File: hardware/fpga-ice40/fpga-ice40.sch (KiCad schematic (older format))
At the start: 74 parts, among them J1 MicroSD_Molex_1040310811, J2 ProgHeader_iCE40, J3 ProgHeader_Flash_QSPI, U1 iCE40HX4K-TQ144, U2 IS42S16320F-6TL, U3 W25Q32JVZP, U4 W25Q32JVZP

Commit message: Use a combined SOIC-8/16W layout for flash ICs
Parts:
- removed U3, U4: W25Q32JVZP, Package_SON:WSON-8-1EP_6x5mm_P1.27mm_EP3.4x4.3mm, symbol ng_memory:W25Q32JVZP
- added U3, U4: W25Q32JVSS, Package_SO:SOIC-8_5.275x5.275mm_P1.27mm, symbol ng_memory:W25Q32JVSS
- added U5, U6: S25FL256SAGMFI01, Package_SO:SOIC-16W_7.5x10.3mm_P1.27mm, symbol ng_memory:S25FL256SAGMFI01
- gave numbers to parts that had none: 37
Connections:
- wire segments 356 -> 374
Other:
- moved on the sheet: C22, C23, C24, J1, J2, J3, R8, RN1, RN2, RN3

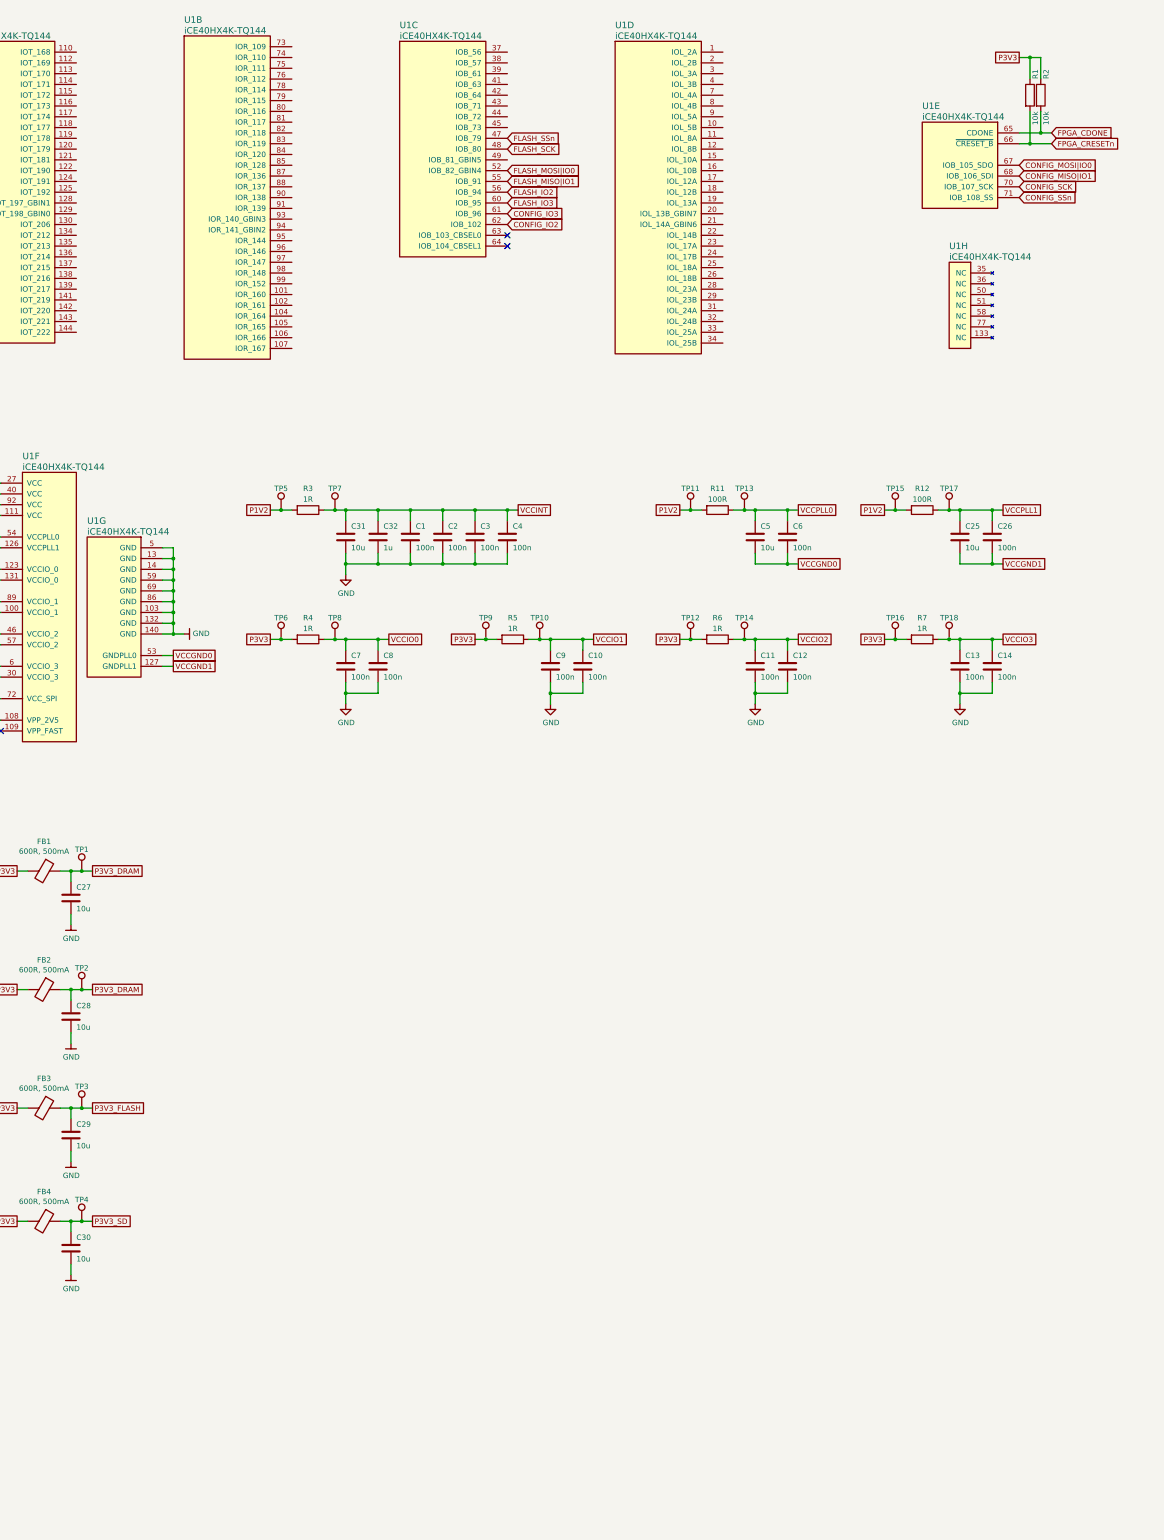
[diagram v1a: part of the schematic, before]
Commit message: Begin pin assignments from FPGA to N64 bus and SDRAM
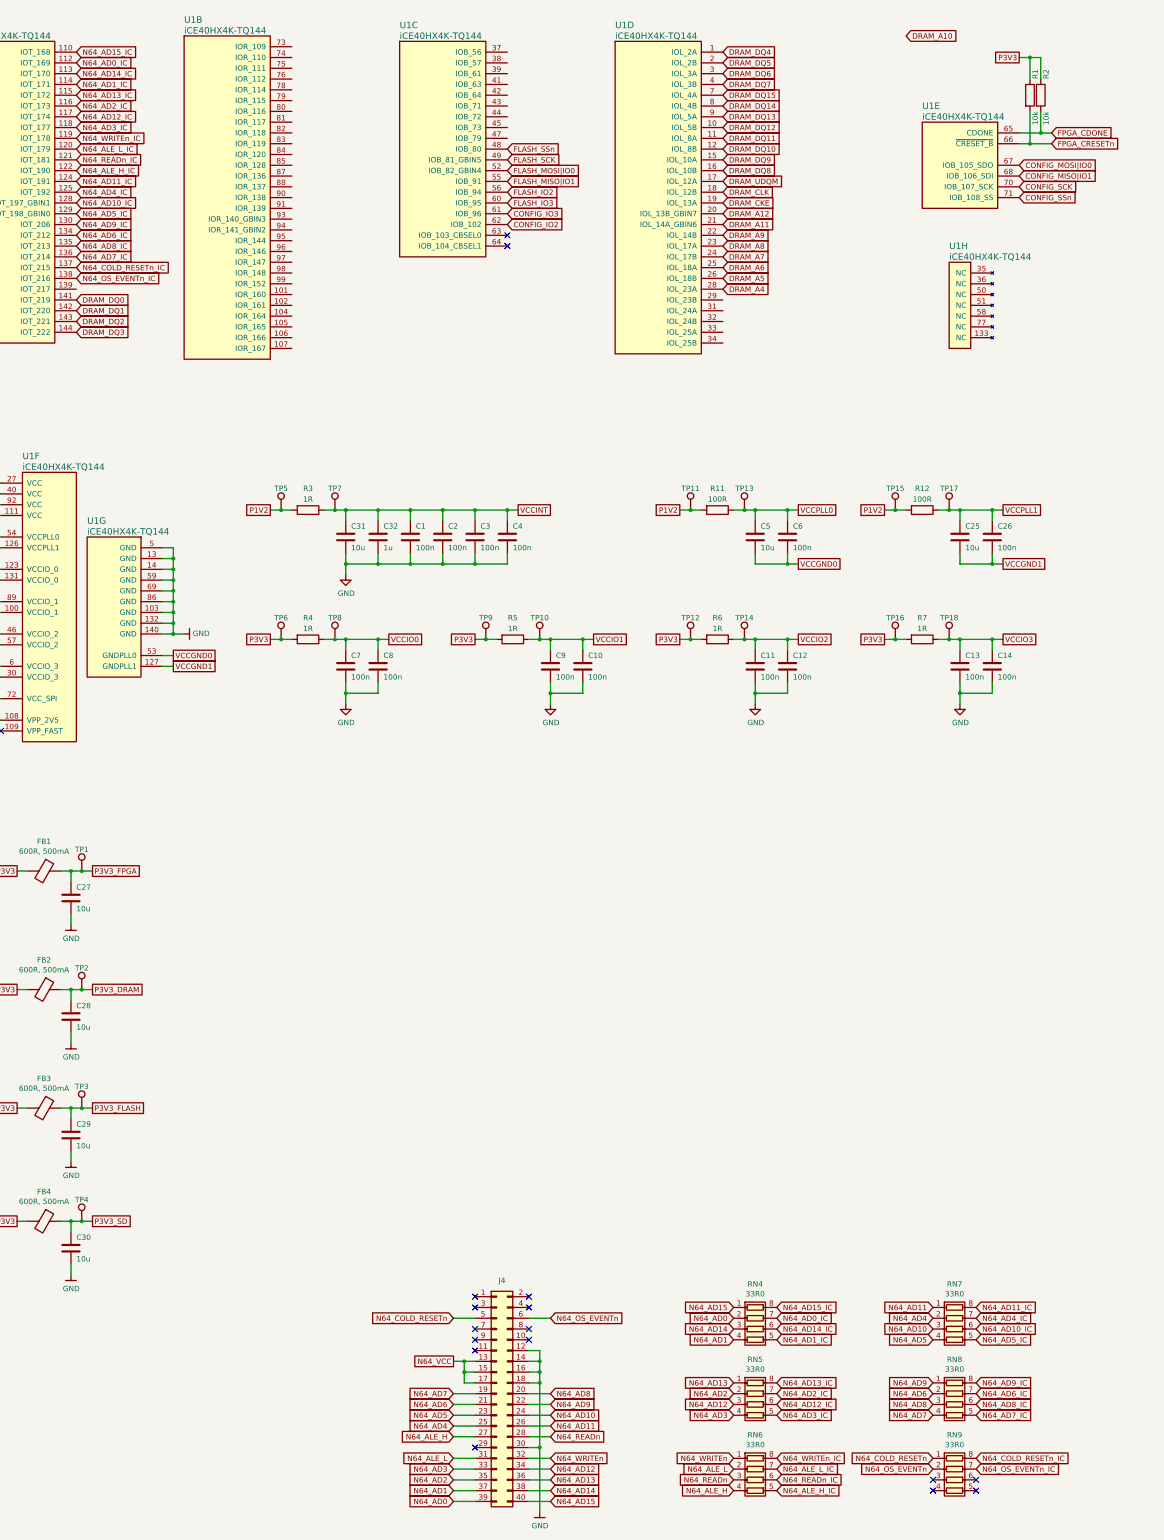
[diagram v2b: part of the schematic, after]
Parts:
- added J4: Conn_02x20_Odd_Even, Connector_PinHeader_2.54mm:PinHeader_2x20_P2.54mm_Horizontal, symbol Connector_Generic:Conn_02x20_Odd_Even
- added RN4, RN5, RN6, RN7, RN8, RN9: 33R0, Resistor_SMD:R_Array_Convex_4x0603, symbol Device:R_Pack04
- RN1, RN2, RN3: footprint (none) -> Resistor_SMD:R_Array_Convex_4x0603
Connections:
- net DRAM_A11: now also U1.21 (IOL_14A_GBIN6)
- net DRAM_A12: now also U1.20 (IOL_13B_GBIN7)
- net DRAM_A4: now also U1.28 (IOL_23A)
- net DRAM_A5: now also U1.26 (IOL_18B)
- net DRAM_A6: now also U1.25 (IOL_18A)
- net DRAM_A7: now also U1.24 (IOL_17B)
- net DRAM_A8: now also U1.23 (IOL_17A)
- net DRAM_A9: now also U1.22 (IOL_14B)
- net DRAM_CKE: now also U1.19 (IOL_13A)
- net DRAM_CLK: now also U1.18 (IOL_12B)
- net DRAM_DQ0: now also U1.141 (IOT_219)
- net DRAM_DQ1: now also U1.142 (IOT_220)
- net DRAM_DQ10: now also U1.12 (IOL_8B)
- net DRAM_DQ11: now also U1.11 (IOL_8A)
- net DRAM_DQ12: now also U1.10 (IOL_5B)
- net DRAM_DQ13: now also U1.9 (IOL_5A)
- net DRAM_DQ14: now also U1.8 (IOL_4B)
- net DRAM_DQ15: now also U1.7 (IOL_4A)
- net DRAM_DQ2: now also U1.143 (IOT_221)
- net DRAM_DQ3: now also U1.144 (IOT_222)
- net DRAM_DQ4: now also U1.1 (IOL_2A)
- net DRAM_DQ5: now also U1.2 (IOL_2B)
- net DRAM_DQ6: now also U1.3 (IOL_3A)
- net DRAM_DQ7: now also U1.4 (IOL_3B)
- net DRAM_DQ8: now also U1.16 (IOL_10B)
- net DRAM_DQ9: now also U1.15 (IOL_10A)
- net DRAM_UDQM: now also U1.17 (IOL_12A)
- net FLASH_SCK: now also U1.49 (IOB_81_GBIN5); no longer U1.48 (IOB_80)
- net FLASH_SSn: now also U1.48 (IOB_80); no longer U1.47 (IOB_79)
- net GND: now also J4.12 (Pin_12), J4.14 (Pin_14), J4.16 (Pin_16), J4.18 (Pin_18), J4.30 (Pin_30)
- net P3V3_DRAM: no longer C27.1, FB1.1, TP1.1
- net N64_AD15_IC: now reaches U1.110 (IOT_168)
- net N64_AD15_IC: now also RN4.8 (R1.2)
- net N64_AD0_IC: now reaches U1.112 (IOT_169)
- net N64_AD0_IC: now also RN4.7 (R2.2)
- net N64_AD14_IC: now reaches U1.113 (IOT_170)
- net N64_AD14_IC: now also RN4.6 (R3.2)
- net N64_AD1_IC: now reaches U1.114 (IOT_171)
- net N64_AD1_IC: now also RN4.5 (R4.2)
- net N64_AD13_IC: now reaches U1.115 (IOT_172)
- net N64_AD13_IC: now also RN5.8 (R1.2)
- net N64_AD2_IC: now reaches U1.116 (IOT_173)
- net N64_AD2_IC: now also RN5.7 (R2.2)
- net N64_AD12_IC: now reaches U1.117 (IOT_174)
- net N64_AD12_IC: now also RN5.6 (R3.2)
- net N64_AD3_IC: now reaches U1.118 (IOT_177)
- net N64_AD3_IC: now also RN5.5 (R4.2)
- net N64_WRITEn_IC: now reaches U1.119 (IOT_178)
- net N64_WRITEn_IC: now also RN6.8 (R1.2)
- net N64_ALE_L_IC: now reaches U1.120 (IOT_179)
- net N64_ALE_L_IC: now also RN6.7 (R2.2)
- net N64_READn_IC: now reaches U1.121 (IOT_181)
- net N64_READn_IC: now also RN6.6 (R3.2)
- net N64_ALE_H_IC: now reaches U1.122 (IOT_190)
- net N64_ALE_H_IC: now also RN6.5 (R4.2)
- net N64_AD11_IC: now reaches U1.124 (IOT_191)
- net N64_AD11_IC: now also RN7.8 (R1.2)
- net N64_AD4_IC: now reaches U1.125 (IOT_192)
- net N64_AD4_IC: now also RN7.7 (R2.2)
- net N64_AD10_IC: now reaches U1.128 (IOT_197_GBIN1)
- net N64_AD10_IC: now also RN7.6 (R3.2)
- net N64_AD5_IC: now reaches U1.129 (IOT_198_GBIN0)
- net N64_AD5_IC: now also RN7.5 (R4.2)
- net N64_AD9_IC: now reaches U1.130 (IOT_206)
- net N64_AD9_IC: now also RN8.8 (R1.2)
- net N64_AD6_IC: now reaches U1.134 (IOT_212)
- net N64_AD6_IC: now also RN8.7 (R2.2)
- net N64_AD8_IC: now reaches U1.135 (IOT_213)
- net N64_AD8_IC: now also RN8.6 (R3.2)
- net N64_AD7_IC: now reaches U1.136 (IOT_214)
- net N64_AD7_IC: now also RN8.5 (R4.2)
- net N64_COLD_RESETn_IC: now reaches U1.137 (IOT_215)
- net N64_COLD_RESETn_IC: now also RN9.8 (R1.2)
- net N64_OS_EVENTn_IC: now reaches U1.138 (IOT_216)
- net N64_OS_EVENTn_IC: now also RN9.7 (R2.2)
- new net N64_AD0: J4.39 (Pin_39), RN4.2 (R2.1)
- new net N64_AD1: J4.37 (Pin_37), RN4.4 (R4.1)
- new net N64_AD10: J4.24 (Pin_24), RN7.3 (R3.1)
- new net N64_AD11: J4.26 (Pin_26), RN7.1 (R1.1)
- new net N64_AD12: J4.34 (Pin_34), RN5.3 (R3.1)
- new net N64_AD13: J4.36 (Pin_36), RN5.1 (R1.1)
- new net N64_AD14: J4.38 (Pin_38), RN4.3 (R3.1)
- new net N64_AD15: J4.40 (Pin_40), RN4.1 (R1.1)
- new net N64_AD2: J4.35 (Pin_35), RN5.2 (R2.1)
- new net N64_AD3: J4.33 (Pin_33), RN5.4 (R4.1)
- new net N64_AD4: J4.25 (Pin_25), RN7.2 (R2.1)
- new net N64_AD5: J4.23 (Pin_23), RN7.4 (R4.1)
- new net N64_AD6: J4.21 (Pin_21), RN8.2 (R2.1)
- new net N64_AD7: J4.19 (Pin_19), RN8.4 (R4.1)
- new net N64_AD8: J4.20 (Pin_20), RN8.3 (R3.1)
- new net N64_AD9: J4.22 (Pin_22), RN8.1 (R1.1)
- new net N64_ALE_H: J4.27 (Pin_27), RN6.4 (R4.1)
- new net N64_ALE_L: J4.31 (Pin_31), RN6.2 (R2.1)
- new net N64_COLD_RESETn: J4.5 (Pin_5), RN9.1 (R1.1)
- new net N64_OS_EVENTn: J4.6 (Pin_6), RN9.2 (R2.1)
- new net N64_READn: J4.28 (Pin_28), RN6.3 (R3.1)
- new net N64_VCC: J4.13 (Pin_13), J4.15 (Pin_15), J4.17 (Pin_17)
- new net N64_WRITEn: J4.32 (Pin_32), RN6.1 (R1.1)
- new net P3V3_FPGA: C27.1, FB1.1, TP1.1
- no-connect marks 4 -> 18

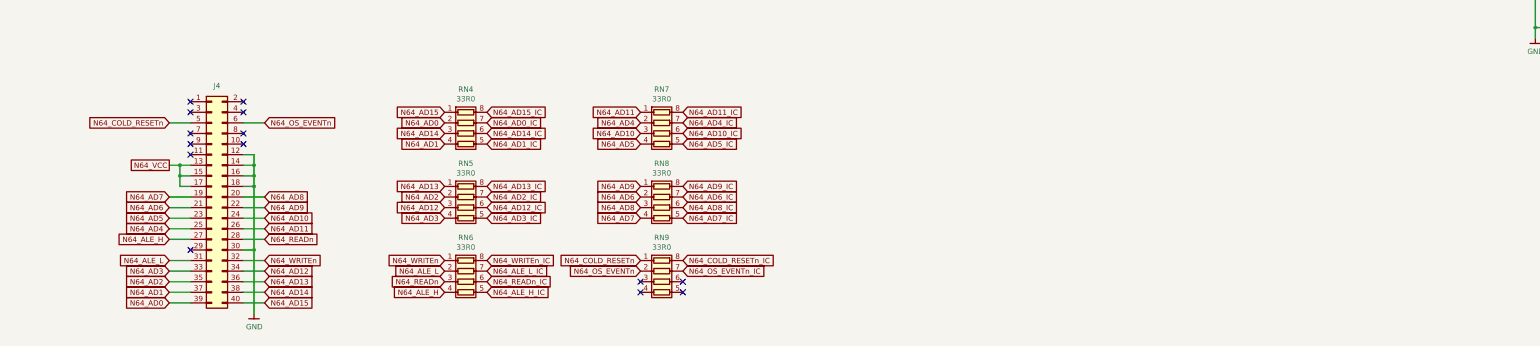
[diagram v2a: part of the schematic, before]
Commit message: Add FT245RL footprint to layout
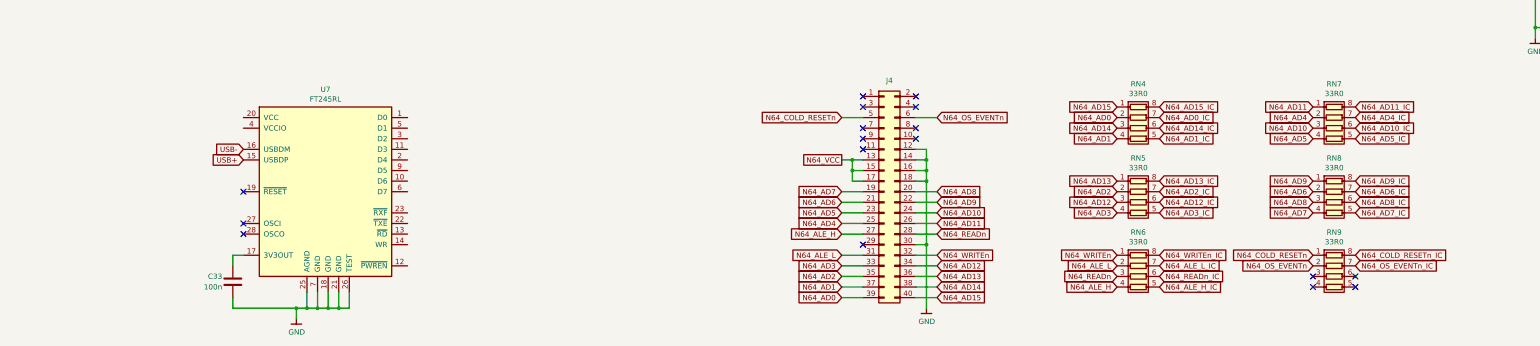
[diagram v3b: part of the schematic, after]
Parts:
- added C33: 100n, Capacitor_SMD:C_0603_1608Metric, symbol Device:C
- added U7: FT245RL, Package_SO:SSOP-28_5.3x10.2mm_P0.65mm, symbol ng_ftdi:FT245RL
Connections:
- net GND: now also C33.2, U7.18 (GND), U7.21 (GND), U7.25 (AGND), U7.26 (TEST), U7.7 (GND)
- new net: C33.1, U7.17 (3V3OUT)
- new net USB+: U7.15 (USBDP)
- new net USB-: U7.16 (USBDM)
- no-connect marks 18 -> 21
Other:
- moved on the sheet: J4, RN4, RN5, RN6, RN7, RN8, RN9
